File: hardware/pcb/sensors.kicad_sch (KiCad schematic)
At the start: 34 parts, among them J4 4-20mA_1, J5 4-20mA_2, J6 DS18B20, J7 Spare, Q2 AO3400A, U9 ADS1115

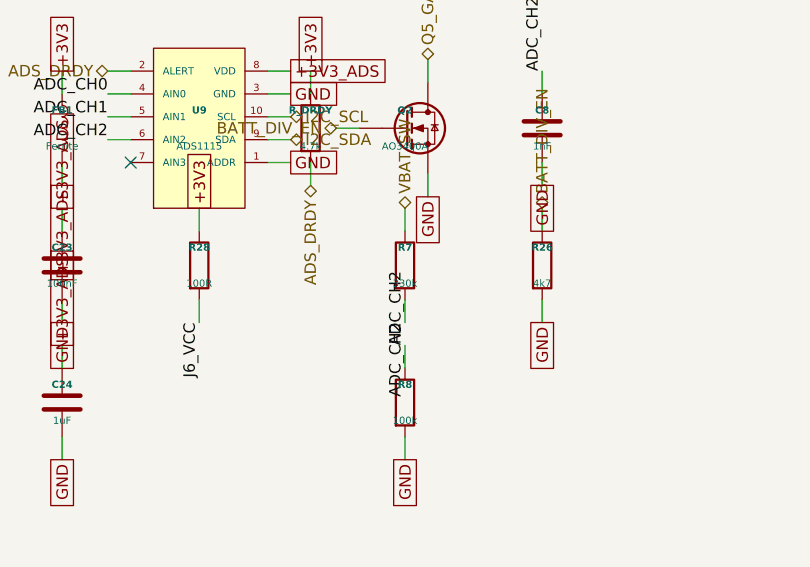
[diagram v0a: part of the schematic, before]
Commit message: hw(pcb): convert power architecture to 1S — TP4056 + CN3791 + HT7333-A
Pack 2S1P -> 1S2P (VBAT 3.0-4.2 V; user decision, chosen over 2S for
simplicity/ecosystem). IP2326 boost subsystem deleted -> TP4056 1 A linear
USB charger; CN3722 + external buck stage deleted -> CN3791 integrated-switch
1S MPPT charger (/CHRG_SOLAR net and GPIO map unchanged); AP63203WU buck
(VIN min 3.8 V) deleted -> HT7333-A LDO. D13 -> SMAJ5.0A, D8/D14 -> SMAJ10CA,
R7 330k -> 100k (/2 divider), F2 footprint 1206 -> 1812 per blocker 8.
Netlist re-verified: 337 pins / 63 nets / 10 NC / zero mismatches.
Docs updated: schematic_connections (new 1S blockers 10a-e), BOM, placement
groups B/D/G/L, fab checklist, component-review addendum, CHANGELOG.

Co-Authored-By: Claude Fable 5 <noreply@anthropic.com>
Claude-Session: https://claude.ai/code/session_01VtMFY5Q94iYbsNPpLcPJyK
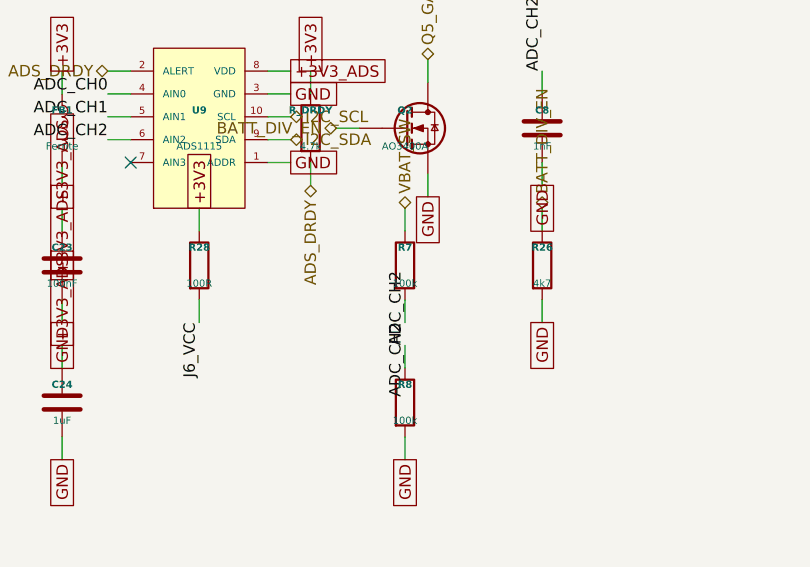
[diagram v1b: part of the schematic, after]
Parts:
- R7: value 330k -> 100k
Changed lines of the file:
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@@
 			)
 		)
-		(property "Value" "330k"
+		(property "Value" "100k"
 			(at 110.49 144.24 0)
 			(show_name no)
